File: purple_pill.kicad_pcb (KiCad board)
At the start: 2 copper layers, 27.9 x 63.5 mm, 35 parts, among them J1 Conn_01x24_MountingPin, J2 Conn_01x24_MountingPin, J3 JTAG_SWD_10, J4 USB_C_Receptacle_USB2.0, U1 STM32F405RGTx, U2 LD1117S33TR_SOT223, X1 8Mhz, X2 32.768KHz

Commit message: PCB Layout Complete
 On branch master
 Changes to be committed:
	modified:   purple_pill.kicad_pcb
	modified:   purple_pill.pro
	modified:   purple_pill.sch
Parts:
- removed C10, C12: 100nF, Capacitor_SMD:C_0805_2012Metric_Pad1.15x1.40mm_HandSolder
- removed JP5: Jumper_NC_Small, Jumper:SolderJumper-2_P1.3mm_Open_TrianglePad1.0x1.5mm
- C1, C2, C3, C4, C5, C6, JP1, JP2, JP4, JP6: moved to B.Cu
- JP3: value Jumper_3_Bridged12 -> BOOT
- moved C2 68.1 mm to (146.4, 127.1)
- moved C7 64.7 mm to (130.8, 125.5), turned to 90 degrees
- moved C4 61.6 mm to (137.9, 100.3), turned to 90 degrees
- moved C3 58.0 mm to (131.3, 100.3), turned to 270 degrees
- moved JP1 55.5 mm to (146.4, 122.0), turned to 180 degrees
- moved C9 54.8 mm to (143.3, 98.7)
- moved C6 53.7 mm to (129.7, 114.3), turned to 270 degrees
- moved C11 52.4 mm to (133.3, 88.6), turned to 90 degrees
- moved C8 52.1 mm to (144.3, 95.0), turned to 90 degrees
- moved C5 51.8 mm to (129.7, 106.4), turned to 90 degrees
- moved C1 44.8 mm to (146.4, 124.6)
- moved JP4 43.7 mm to (138.7, 111.0)
- moved JP6 38.9 mm to (138.7, 114.8)
- moved JP2 35.9 mm to (146.4, 129.7), turned to 180 degrees
- moved R7 33.4 mm to (146.8, 88.6), turned to 270 degrees
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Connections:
- J1 pad 23: GNDA -> GND
- J2 pad 23: GNDA -> GND
- U1 pad 12: GNDA -> GND
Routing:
- net GND: track 0.00 -> 69.6 mm, vias 0 -> 22
- net /PC0: track 0.00 -> 44.0 mm, vias 0 -> 1
- net /PC1: track 0.00 -> 41.9 mm, vias 0 -> 1
- net /PA0: track 0.00 -> 40.2 mm
- net /PB4: track 0.00 -> 39.9 mm, vias 0 -> 1
- net /PC2: track 0.00 -> 39.9 mm, vias 0 -> 1
- net /PC3: track 0.00 -> 38.6 mm, vias 0 -> 1
- net /PA1: track 0.00 -> 38.1 mm
- net /PA2: track 0.00 -> 37.9 mm, vias 0 -> 1
- net /PA4: track 0.00 -> 37.1 mm
- net /PA3: track 0.00 -> 36.3 mm
- net Net-(R2-Pad1): track 0.00 -> 35.4 mm
- net /PC4: track 0.00 -> 34.9 mm, vias 0 -> 1
- net /PA6: track 0.00 -> 34.3 mm, vias 0 -> 1
- net +3V3: track 0.00 -> 33.6 mm, vias 0 -> 16
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- added copper zone on 3v3, net +3V3
- added copper zone on GND, net GND
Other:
- copper layers 2 -> 4
- net class Default: clearance 0.2 -> 0.1524; trace_width 0.25 -> 0.1524; via_dia 0.8 -> 0.6604; via_drill 0.4 -> 0.254
- net class Gnd added: clearance 0.1524, trace_width 0.254, via_dia 0.6604, via_drill 0.254
- net class Power added: clearance 0.1524, trace_width 0.254, via_dia 0.6604, via_drill 0.254
- rule pad_to_mask_clearance: 0.051 -> 0.0254
- rule solder_mask_min_width: 0.25 -> 0.0254
- rule trace_clearance: 0.2 -> 0.1524
- rule trace_min: 0.2 -> 0.1524
- rule via_min_drill: 0.3 -> 0.254
- rule via_min_size: 0.4 -> 0.6604
- board text added: "Purple Pill 1.0"
- board text added: "https://github.com/jboard146/PurplePill"

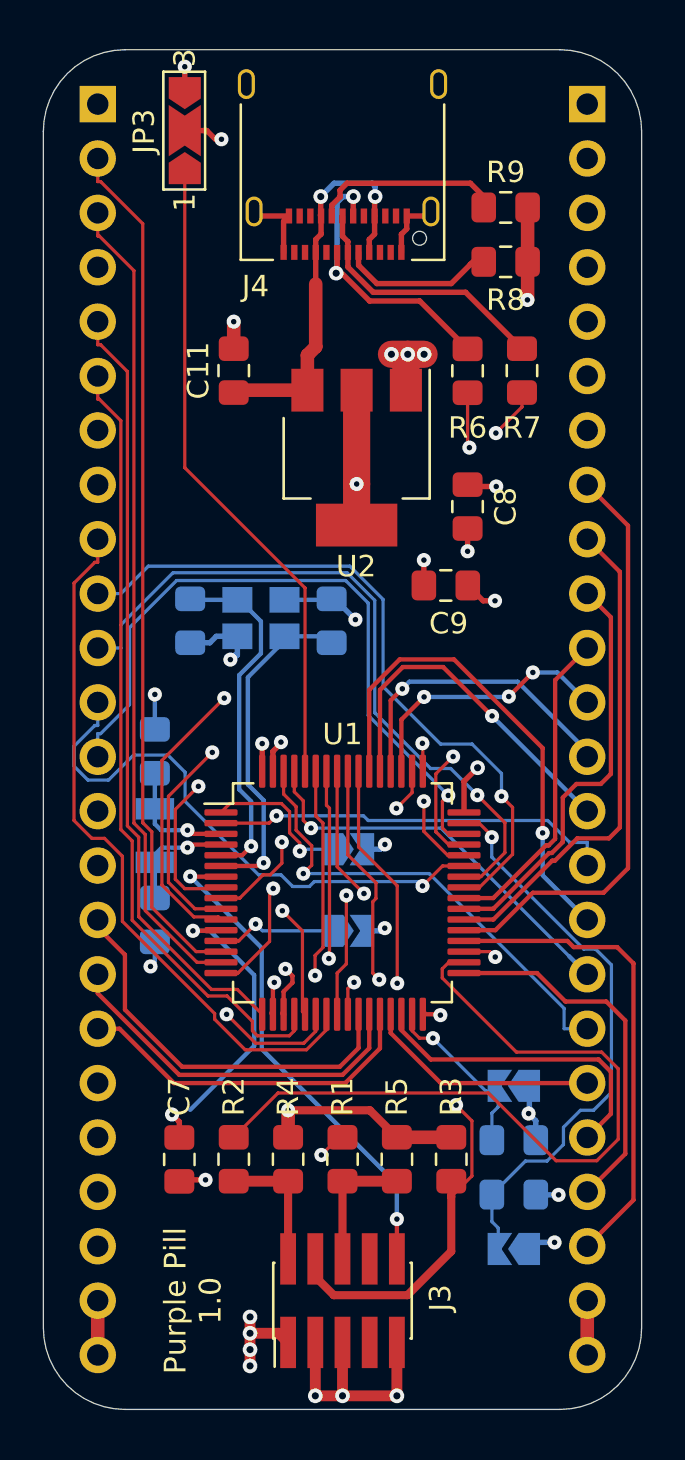
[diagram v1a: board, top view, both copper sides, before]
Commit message: Re-Ran AutoRoute
 On branch master
 Changes to be committed:
	modified:   purple_pill.kicad_pcb
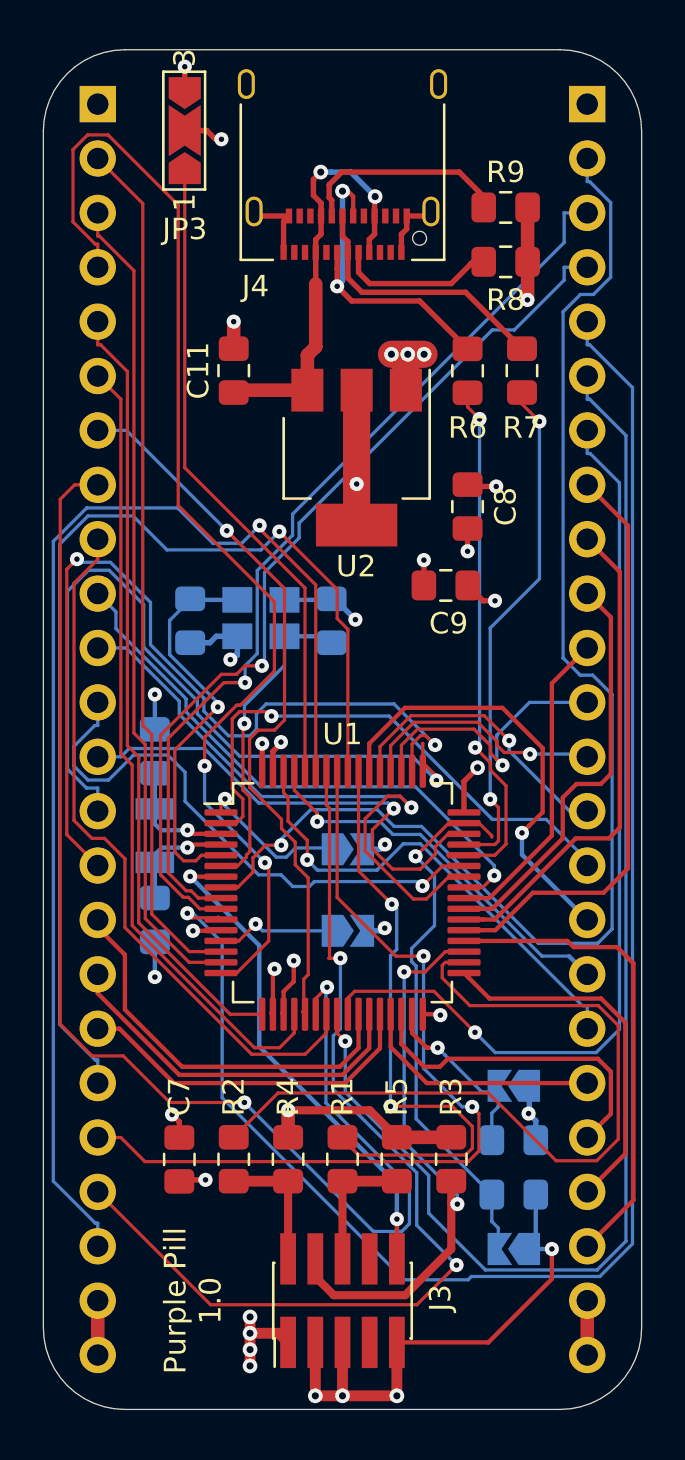
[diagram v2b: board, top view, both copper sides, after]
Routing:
- net /PC3: track 38.6 -> 78.6 mm
- net /PB7: track 28.6 -> 57.7 mm
- net /PC4: track 34.9 -> 63.1 mm
- net /PA6: track 34.3 -> 61.2 mm, vias 1 -> 2
- net /PB6: track 24.8 -> 45.9 mm, vias 1 -> 2
- net /PA15: track 20.8 -> 41.3 mm, vias 1 -> 2
- net /PC0: track 44.0 -> 62.3 mm
- net /PA2: track 37.9 -> 54.4 mm, vias 1 -> 2
- net /PB5: track 23.8 -> 40.0 mm, vias 1 -> 2
- net /PA14: track 23.7 -> 36.8 mm
- net /PC5: track 33.2 -> 43.9 mm
- net /PB4: track 39.9 -> 50.3 mm
- net /PA13: track 32.5 -> 23.0 mm
- net Net-(R1-Pad1): track 21.5 -> 28.5 mm
- net /PC13: track 18.8 -> 25.8 mm
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
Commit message: Minor Edits
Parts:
- C11, C8: footprint Capacitor_SMD:C_0805_2012Metric_Pad1.15x1.40mm_HandSolder -> Capacitor_SMD:C_1210_3225Metric_Pad1.42x2.65mm_HandSolder
- moved C9 1.01 mm to (144.3, 98.7)
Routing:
- net GND: track 70.6 -> 88.5 mm, vias 21 -> 28
- net +3V3: track 33.9 -> 50.6 mm, vias 16 -> 24
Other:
- board text added: "3V3"
- board text added: "A0"
- board text added: "A1"
- board text added: "A12"
- board text added: "A13"
- board text added: "A14"
- board text added: "A15"
- board text added: "A2"
- board text added: "A3"
- board text added: "A4"
- board text added: "A5"
- board text added: "A6"
- board text added: "A7"
- board text added: "A8"
- board text added: "A9"
- board text added: "B0"
- board text added: "B1"
- board text added: "B10"
- board text added: "B11"
- board text added: "B12"
- board text added: "B15"
- board text added: "B2"
- board text added: "B4"
- board text added: "B5"
- board text added: "B6"
- board text added: "B7"
- board text added: "B8"
- board text added: "B9"
- board text added: "C0"
- board text added: "C1"
- board text added: "C10"
- board text added: "C11"
- board text added: "C12"
- board text added: "C13"
- board text added: "C2"
- board text added: "C3"
- board text added: "C4"
- board text added: "C5"
- board text added: "C6"
- board text added: "C7"
- board text added: "C8"
- board text added: "C9"
- board text added: "D12"
- board text added: "GND"
